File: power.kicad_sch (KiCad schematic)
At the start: 24 parts, among them J2 Barrel_Jack_MountingPin, U1 ST715M25R, U3 ZXCT1107

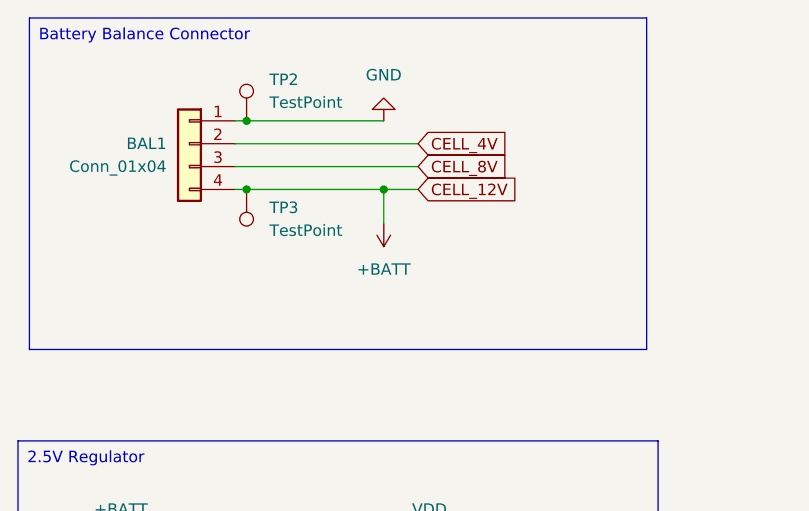
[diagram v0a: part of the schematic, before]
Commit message: Some part selections
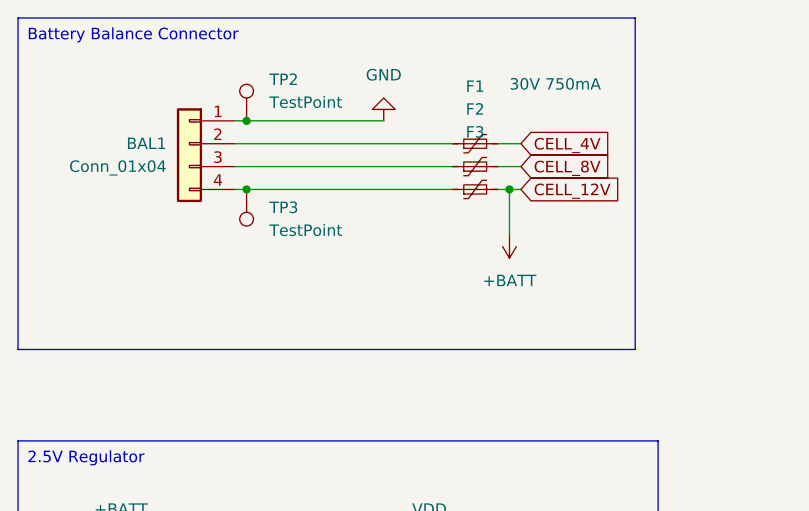
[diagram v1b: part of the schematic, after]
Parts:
- added F1, F2, F3: 30V 750mA, Fuse:Fuse_1206_3216Metric, symbol Device:Polyfuse_Small
- J2: footprint Connector_BarrelJack:BarrelJack_CUI_PJ-063AH_Horizontal -> Connector_BarrelJack:BarrelJack_Horizontal; LCSC_Code (none) -> C319099
- R5: footprint (none) -> Resistor_SMD:R_0603_1608Metric
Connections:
- net +BATT: now also F3.2; no longer BAL1.4 (Pin_4), TP3.1
- net CELL_4V: now also F1.2; no longer BAL1.2 (Pin_2)
- net CELL_8V: now also F2.2; no longer BAL1.3 (Pin_3)
- new net: BAL1.4 (Pin_4), F3.1, TP3.1
- new net: BAL1.2 (Pin_2), F1.1
- new net: BAL1.3 (Pin_3), F2.1

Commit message: Text
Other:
- note added: "Rsense = .25 ohm, @ 2 amps = 0.5V Iout = 0.004 * Vsense so 1200 * 0.002 = 2.4V @ 2 amps current"
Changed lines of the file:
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@@
+		)
+	)
+	(text "Rsense = .25 ohm, @ 2 amps = 0.5V\nIout = 0.004 * Vsense\nso 1200 * 0.002 = 2.4V @ 2 amps current"
+		(exclude_from_sim no)
+		(at 220.218 36.068 0)
+		(effects
+			(font
+				(size 1.27 1.27)
+			)
 		)
 	)

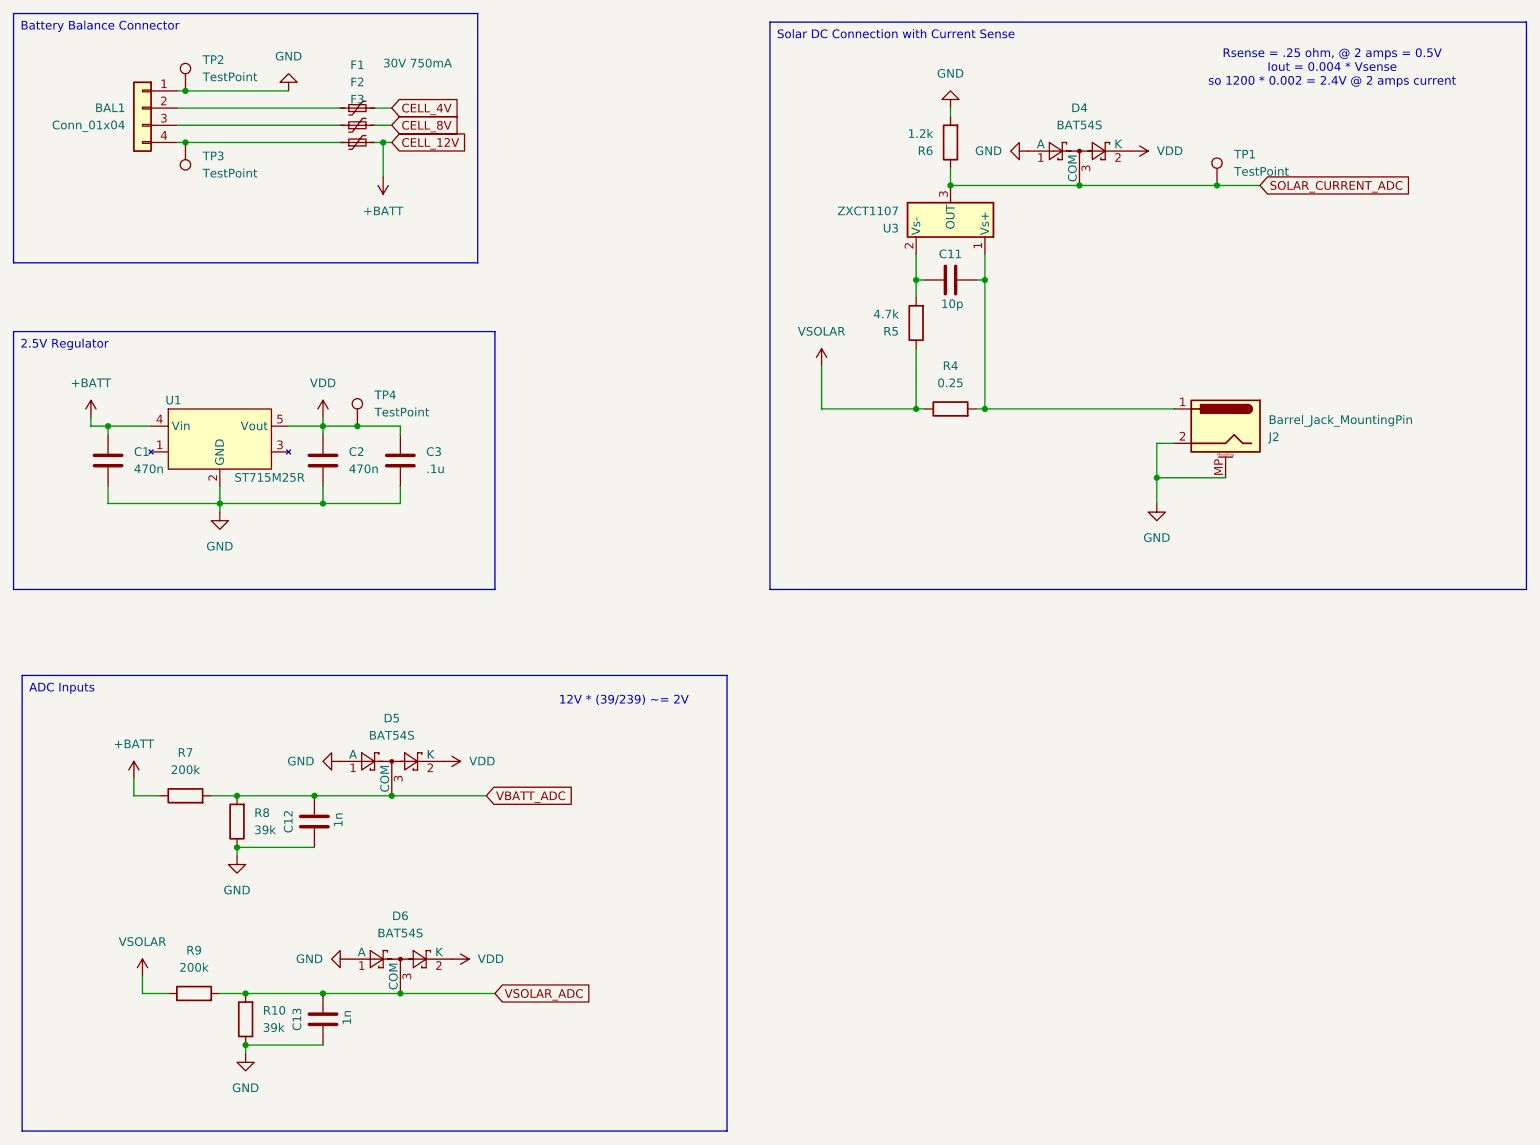
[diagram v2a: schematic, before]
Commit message: Smaller diodes, more work
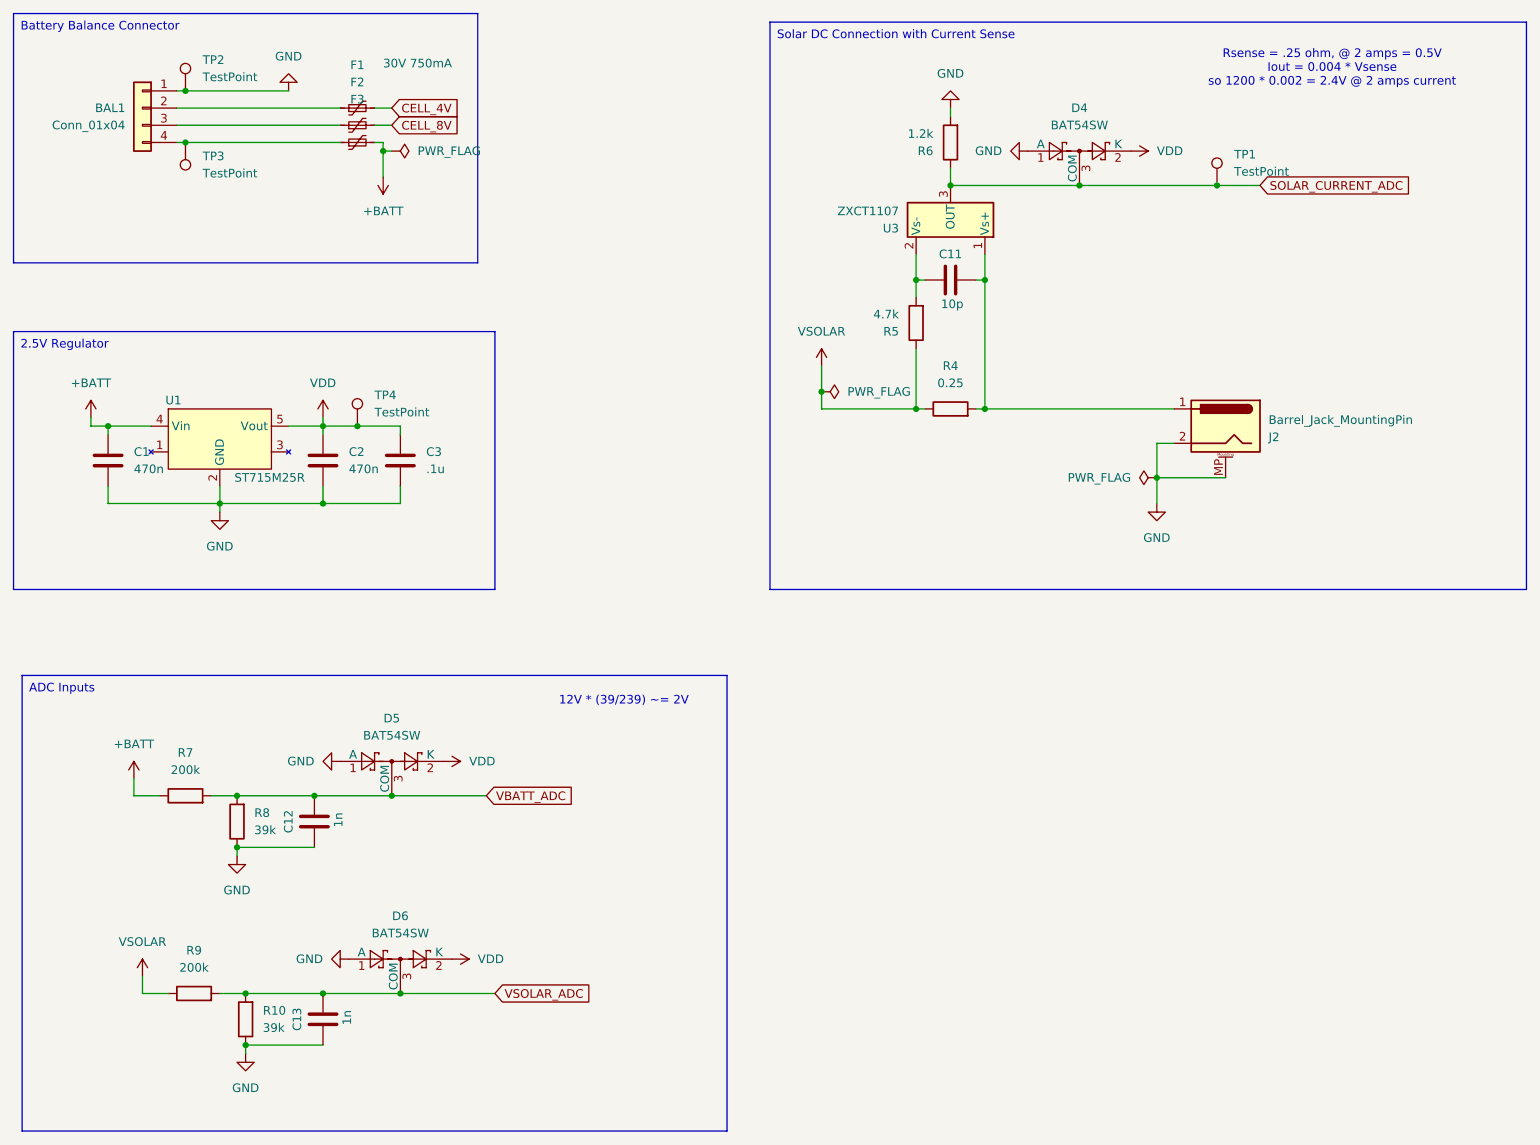
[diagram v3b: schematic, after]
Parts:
- removed D4, D5, D6: BAT54S, Package_TO_SOT_SMD:SOT-23, symbol Diode:BAT54S
- added D4, D5, D6: BAT54SW, Package_TO_SOT_SMD:SOT-323_SC-70, symbol Diode:BAT54SW
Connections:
- net GND: now also D4.1 (A), D5.1 (A), D6.1 (A)
- net SOLAR_CURRENT_ADC: now also D4.3 (COM)
- net VBATT_ADC: now also D5.3 (COM)
- net VDD: now also D4.2 (K), D5.2 (K), D6.2 (K)
- net VSOLAR_ADC: now also D6.3 (COM)

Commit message: More layout adust
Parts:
- added C14, C15: 10u, Capacitor_SMD:C_1206_3216Metric, symbol Device:C
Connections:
- net GND: now also C14.2, C15.2
- net at C11.1, J2.1, R4.2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: now also C14.1, C15.1

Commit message: Routing
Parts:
- TP1: value TestPoint -> SOLAR_CUR
- TP2: value TestPoint -> GND
- TP3: value TestPoint -> +BATT
- TP4: value TestPoint -> VDD
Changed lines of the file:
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@@
 			)
 		)
-		(property "Value" "TestPoint"
+		(property "Value" "VDD"
 			(at 78.74 86.8679 0)
 			(effects
@@
 			)
 		)
-		(property "Value" "TestPoint"
+		(property "Value" "+BATT"
 			(at 53.34 51.5619 0)
 			(effects
@@
 			)
 		)
-		(property "Value" "TestPoint"
+		(property "Value" "GND"
 			(at 53.34 37.3379 0)
 			(effects
@@
 			)
 		)
-		(property "Value" "TestPoint"
+		(property "Value" "SOLAR_CUR"
 			(at 205.74 51.3079 0)
 			(effects

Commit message: bom pt1
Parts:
- BAL1: LCSC_Code (none) -> C157925
- C11: LCSC_Code (none) -> C1634
- C14, C15: LCSC_Code C15850 -> C13585
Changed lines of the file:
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@@
 			)
 		)
-		(property "LCSC_Code" "C15850"
+		(property "LCSC_Code" "C13585"
 			(at 185.42 90.17 0)
 			(effects
@@
 			)
 		)
+		(property "LCSC_Code" "C157925"
+			(at 44.45 41.91 0)
+			(effects
+				(font
+					(size 1.27 1.27)
+				)
+				(hide yes)
+			)
+		)
 		(pin "3"
 		)
@@
 			)
 		)
-		(property "LCSC_Code" "C15850"
+		(property "LCSC_Code" "C13585"
 			(at 177.8 90.17 0)
 			(effects
@@
 			(at 163.83 67.31 0)
 			(effects
+				(font
+					(size 1.27 1.27)
+				)
+				(hide yes)
+			)
+		)
+		(property "LCSC_Code" "C1634"
+			(at 163.83 67.31 0)
+			(effects

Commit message: Assigning PNs
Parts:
- C12, C13: LCSC_Code (none) -> C1588
- D4, D5, D6: LCSC_Code (none) -> C78606
- R10, R8: LCSC_Code (none) -> C23153
- R5: LCSC_Code (none) -> C23162
- R6: LCSC_Code (none) -> C22765
- R7, R9: LCSC_Code (none) -> C25811
- U1: LCSC_Code (none) -> C2832805
- U3: LCSC_Code (none) -> C82766
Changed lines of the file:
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@@
+			)
+		)
+		(property "LCSC_Code" "C78606"
+			(at 82.55 167.64 0)
+			(effects
+				(font
+					(size 1.27 1.27)
+				)
+				(hide yes)
 			)
 		)
@@
 			)
 		)
+		(property "LCSC_Code" "C23153"
+			(at 59.69 176.53 0)
+			(effects
+				(font
+					(size 1.27 1.27)
+				)
+				(hide yes)
+			)
+		)
 		(pin "2"
 		)
@@
 			)
 		)
+		(property "LCSC_Code" "C2832805"
+			(at 48.26 86.36 0)
+			(effects
+				(font
+					(size 1.27 1.27)
+				)
+				(hide yes)
+			)
+		)
 		(pin "2"
 		)
@@
 			)
 		)
+		(property "LCSC_Code" "C1588"
+			(at 69.85 147.32 0)
+			(effects
+				(font
+					(size 1.27 1.27)
+				)
+				(hide yes)
+			)
+		)
 		(pin "2"
 		)
@@
 			)
 		)
+		(property "LCSC_Code" "C25811"
+			(at 52.07 172.72 0)
+			(effects
+				(font
+					(size 1.27 1.27)
+				)
+				(hide yes)
+			)
+		)
 		(pin "2"
 		)
@@
 			)
 		)
+		(property "LCSC_Code" "C82766"
+			(at 163.83 58.42 0)
+			(effects
+				(font
+					(size 1.27 1.27)
+				)
+				(hide yes)
+			)
+		)
 		(pin "1"
 		)
@@
 		)
 		(property "Description" "Resistor"
+			(at 50.8 143.51 0)
+			(effects
+				(font
+					(size 1.27 1.27)
+				)
+				(hide yes)
+			)
+		)
+		(property "LCSC_Code" "C25811"
 			(at 50.8 143.51 0)
 			(effects
@@
 			)
 		)
+		(property "LCSC_Code" "C22765"
+			(at 163.83 46.99 0)
+			(effects
+				(font
+					(size 1.27 1.27)
+				)
+				(hide yes)
+			)
+		)
 		(pin "1"
 		)
@@
 			)
 		)
+		(property "LCSC_Code" "C78606"
+			(at 81.28 138.43 0)
+			(effects
+				(font
+					(size 1.27 1.27)
+				)
+				(hide yes)
+			)
+		)
 		(pin "1"
 		)
@@
 			)
 		)
+		(property "LCSC_Code" "C78606"
+			(at 182.88 48.26 0)
+			(effects
+				(font
+					(size 1.27 1.27)
+				)
+				(hide yes)
+			)
+		)
 		(pin "1"
 		)
@@
 			)
 		)
+		(property "LCSC_Code" "C23162"
+			(at 158.75 73.66 0)
+			(effects
+				(font
+					(size 1.27 1.27)
+				)
+				(hide yes)
+			)
+		)
 		(pin "2"
 		)
@@
 			)
 		)
+		(property "LCSC_Code" "C23153"
+			(at 58.42 147.32 0)
+			(effects
+				(font
+					(size 1.27 1.27)
+				)
+				(hide yes)
+			)
+		)
 		(pin "2"
 		)
@@
 			(at 71.12 176.53 0)
 			(effects
+				(font
+					(size 1.27 1.27)
+				)
+				(hide yes)
+			)
+		)
+		(property "LCSC_Code" "C1588"
+			(at 71.12 176.53 0)
+			(effects

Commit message: slight changes
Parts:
- removed C3: .1u, Capacitor_SMD:C_0603_1608Metric, symbol Device:C
- C1: value 470n -> 10u; LCSC_Code (none) -> C13585
- C2: value 470n -> 47u; LCSC_Code (none) -> C96123
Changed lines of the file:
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@@
 	)
 	(junction
-		(at 71.12 100.33)
-		(diameter 0)
-		(color 0 0 0 0)
-	)
-	(junction
-		(at 76.2 88.9)
-		(diameter 0)
-		(color 0 0 0 0)
-	)
-	(junction
 		(at 203.2 53.34)
 		(diameter 0)
@@
 	(wire
 		(pts
-			(xy 76.2 88.9) (xy 82.55 88.9)
-		)
-		(stroke
-			(width 0)
-			(type default)
-		)
-	)
-	(wire
-		(pts
 			(xy 194.31 96.52) (xy 200.66 96.52)
 		)
@@
 	(wire
 		(pts
-			(xy 82.55 100.33) (xy 82.55 97.79)
-		)
-		(stroke
-			(width 0)
-			(type default)
-		)
-	)
-	(wire
-		(pts
 			(xy 43.18 143.51) (xy 43.18 140.97)
 		)
@@
 	(wire
 		(pts
-			(xy 82.55 88.9) (xy 82.55 90.17)
-		)
-		(stroke
-			(width 0)
-			(type default)
-		)
-	)
-	(wire
-		(pts
 			(xy 46.99 143.51) (xy 43.18 143.51)
 		)
@@
 	(wire
 		(pts
-			(xy 71.12 100.33) (xy 82.55 100.33)
-		)
-		(stroke
-			(width 0)
-			(type default)
-		)
-	)
-	(wire
-		(pts
 			(xy 44.45 172.72) (xy 44.45 170.18)
 		)
@@
 			)
 		)
-		(property "Value" "470n"
+		(property "Value" "47u"
 			(at 74.93 95.2499 0)
 			(effects
@@
 			)
 		)
+		(property "LCSC_Code" "C96123"
+			(at 71.12 93.98 0)
+			(effects
+				(font
+					(size 1.27 1.27)
+				)
+				(hide yes)
+			)
+		)
 		(pin "1"
 		)
@@
 			)
 		)
-		(property "Value" "470n"
+		(property "Value" "10u"
 			(at 43.18 95.2499 0)
 			(effects
@@
 			)
 		)
+		(property "LCSC_Code" "C13585"
+			(at 39.37 93.98 0)
+			(effects
+				(font
+					(size 1.27 1.27)
+				)
+				(hide yes)
+			)
+		)
 		(pin "1"
 		)
@@
 					(unit 1)
 				)
-			)
-		)
-	)
-	(symbol
-		(lib_id "Device:C")
-		(at 82.55 93.98 0)
-		(unit 1)
-		(exclude_from_sim no)
-		(in_bom yes)
-		(on_board yes)
-		(dnp no)
-		(fields_autoplaced yes)
-		(property "Reference" "C3"
-			(at 86.36 92.7099 0)
-			(effects
-				(font
-					(size 1.27 1.27)
-				)
-				(justify left)
-			)
-		)
-		(property "Value" ".1u"
-			(at 86.36 95.2499 0)
-			(effects
-				(font
-					(size 1.27 1.27)
-				)
-				(justify left)
-			)
-		)
-		(property "Footprint" "Capacitor_SMD:C_0603_1608Metric"
-			(at 83.5152 97.79 0)
-			(effects
-				(font
-					(size 1.27 1.27)
-				)
-				(hide yes)
-			)
-		)
-		(property "Datasheet" "~"
-			(at 82.55 93.98 0)
-			(effects
-				(font
-					(size 1.27 1.27)
-				)
-				(hide yes)
-			)
-		)
-		(property "Description" "Unpolarized capacitor"
-			(at 82.55 93.98 0)
-			(effects
-				(font
-					(size 1.27 1.27)
-				)
-				(hide yes)
-			)
-		)
-		(property "LCSC_Code" "C14663"
-			(at 82.55 93.98 0)
-			(effects
-				(font
-					(size 1.27 1.27)
-				)
-				(hide yes)
-			)
-		)
-		(pin "1"
-		)
-		(pin "2"
-		)
-		(instances
-			(project "JPBms2"
-				(path "/d86e471c-a8be-422d-a5d1-5a4699b7b766/fda7e15b-dad1-4f54-abdb-4d4569bf33a6"
-					(reference "C3")
-					(unit 1)
-				)
